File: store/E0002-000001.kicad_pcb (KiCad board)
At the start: 2 copper layers, 104.9 x 47 mm, 19 parts, among them J6 Seansor_Header_A, J7 Seansor_Header_B, U1 SHT45-AD1F-R2, U2 BME688, U3 SCD41-D-R2, U4 TLV70018, U5 NCP114

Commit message: M01: name the E0002 power nets GND and +3.3V
The straps are hard-tied to the rails (ADR-0014 d5), and the STRAP_x
global labels outranked the power symbols: the ground plane was named
STRAP_1, the 3V3 rail STRAP_0, and no GND net existed. The labels and
the tie block are removed; J7 pins 3, 4 and 5 tie to +3.3V, GND and GND
directly, with the strap pattern kept as schematic text.

Connectivity unchanged: 93 of 93 pad-to-net assignments identical under
the rename. ERC 21 -> 19, losing the two multiple_net_names warnings.
PCB nets renamed to match; DRC unchanged, parity clean.

Signed-off-by: IIchukissII <133657307+IIchukissII@users.noreply.github.com>
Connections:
- net STRAP_0 renamed +3.3V
- net STRAP_1 renamed GND

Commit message: Revert "M01: name the E0002 power nets GND and +3.3V"
This reverts f28e02d. The STRAP_x labels are back on the schematic and the
PCB nets are STRAP_1 and STRAP_0 again, at the same 168 and 70 references.

Also stores the DRC exclusion in the [key, comment] form KiCad itself
writes, replacing the bare string.

Signed-off-by: IIchukissII <133657307+IIchukissII@users.noreply.github.com>
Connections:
- net +3.3V renamed STRAP_0
- net GND renamed STRAP_1

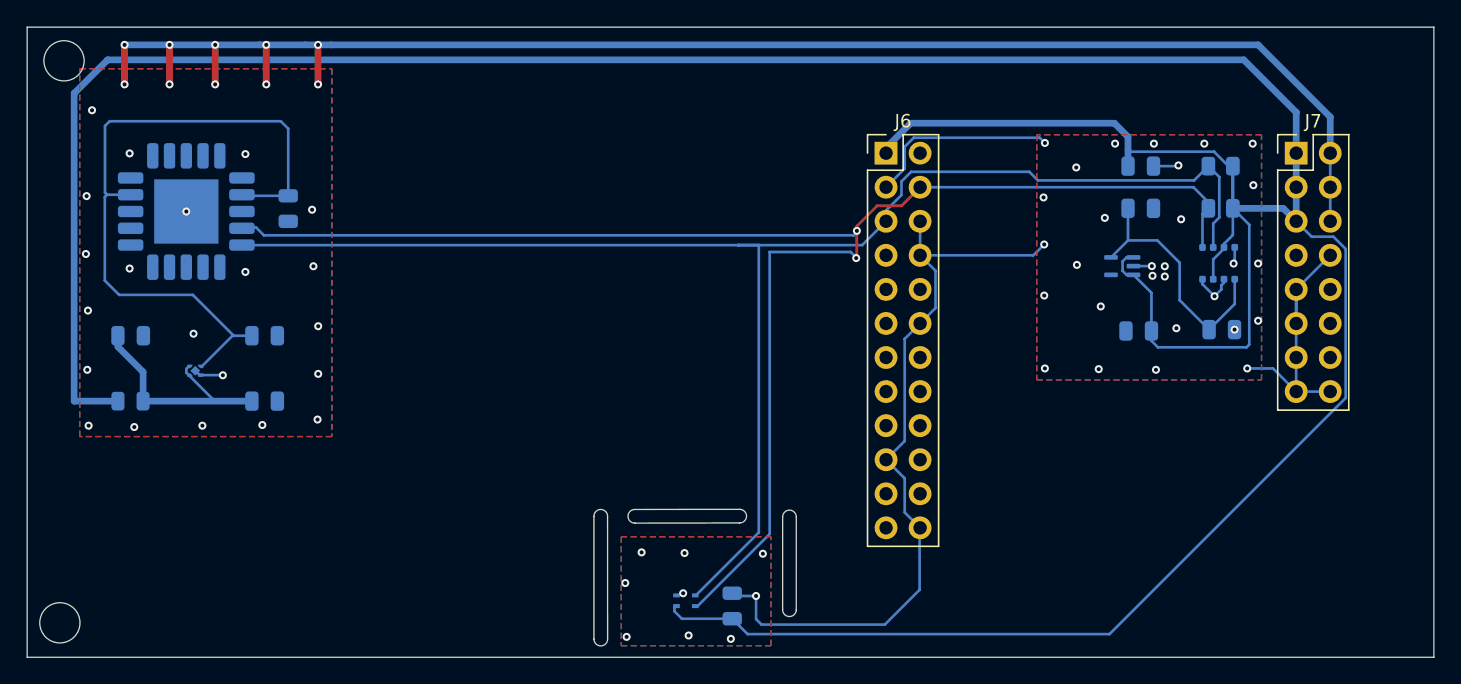
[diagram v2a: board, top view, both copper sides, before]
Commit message: M01: strap J7 pad 5 to GND so the module ID reads 0x01
Pad 5 carries module-ID bit 2 and was on the 3V3 net, which set the bit and
made the strap read 0b101 = 0x05 - the ID of M05-SAFETY, already fabricated
as E0006. The schematic had it on GND all along.

Pad 5 was also the only junction joining three parts of the 3V3 net, so both
branches are re-anchored to pad 3: the 0.5 mm trunk leaves pad 3 down-left to
the existing node at 170.2772,87.2744, and the 0.2 mm feed to U1 drops at
x=169.6772 to clear pad 5 before rejoining at 172.3904,89.3876. Pad 5 is
stitched across to pad 6 on GND.

Verified with zones refilled: 0 DRC violations, and parity drops from 4 to 3
as the net_conflict clears. The unconnected GND stub between pads 6 and 8 is
unchanged - the 3V3 feed to U1 crosses that column and still blocks it.

Signed-off-by: IIchukissII <133657307+IIchukissII@users.noreply.github.com>
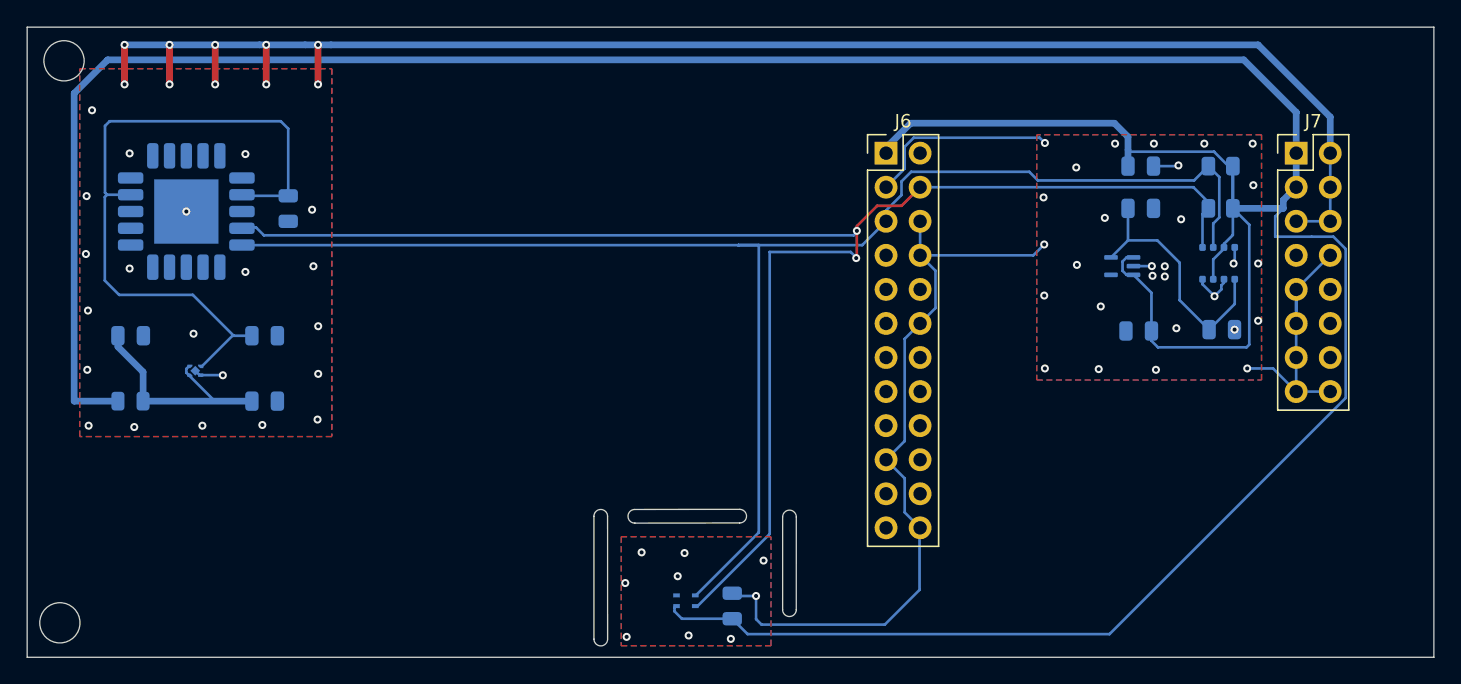
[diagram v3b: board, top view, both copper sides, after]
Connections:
- J7 pad 5: STRAP_0 -> STRAP_1
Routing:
- net STRAP_1: track 216.0 -> 218.5 mm
- net STRAP_0: track 276.1 -> 277.6 mm

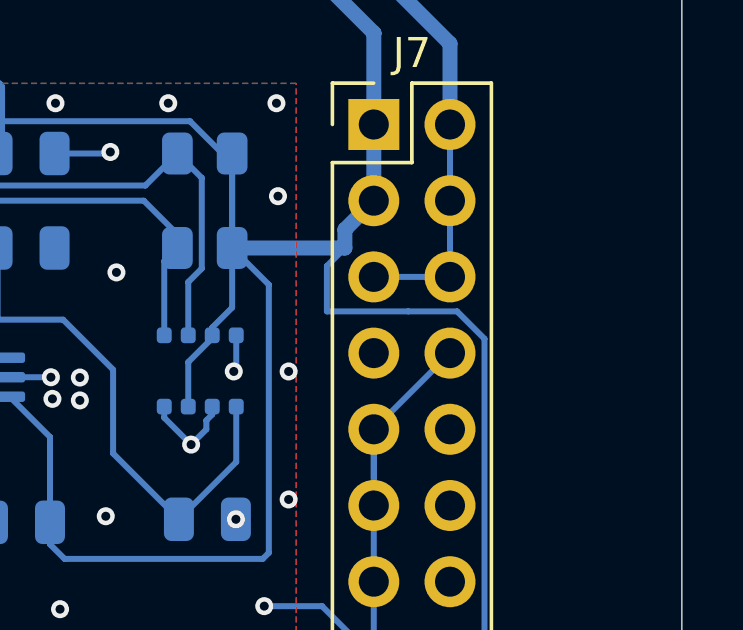
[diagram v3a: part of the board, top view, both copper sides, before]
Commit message: M01: bridge the J7 GND column on F.Cu
The 0.2 mm 3V3 feed to U1 crosses the even pad column on B.Cu at y=89.3876,
which left J7 pads 6 and 8 on separate GND islands. A 0.2 mm F.Cu run between
them clears it. J7 is a through-hole header, so its pads already reach F.Cu
and no vias are needed.

Verified with zones refilled: 0 DRC violations and 0 unconnected items. The
three remaining parity warnings are footprint Value fields holding the
reference designator.

Signed-off-by: IIchukissII <133657307+IIchukissII@users.noreply.github.com>
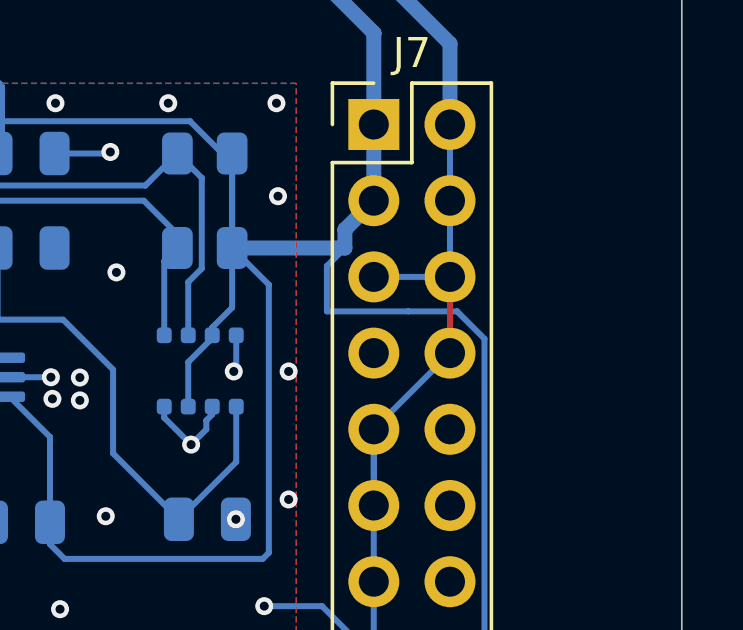
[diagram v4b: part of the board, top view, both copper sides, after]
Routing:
- net STRAP_1: track 218.5 -> 221.1 mm
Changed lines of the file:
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@@
+		(net "STRAP_1")
+	)
+	(segment
+		(start 173.7804 88.2376)
+		(end 173.7804 90.7776)
+		(width 0.2)
+		(layer "F.Cu")
 		(net "STRAP_1")
 	)

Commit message: M01: add the E0002 silkscreen logo and E-number
Copies the LOGO footprint and the E-number / SN text from E0006-000001, in
the arrangement that board uses: version and SN above the mark.

E0001 and E0006 carry all their parts on F.Cu and put the silkscreen on
F.SilkS. E0002 is the other way up - 17 of its 19 footprints are on B.Cu and
the front holds only J6 and J7 - so the block goes on B.SilkS, keeping it on
the component side. The footprint geometry is mirrored and the text carries
the mirror justify, so both read correctly on the back.

Placed at 118,95, in the clear area between the J6 column and the U3 group.
DRC unchanged at 0 violations and 0 unconnected, with no silk_over_copper,
silk_overlap or silk_edge_clearance warnings.

Signed-off-by: IIchukissII <133657307+IIchukissII@users.noreply.github.com>
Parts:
- added G***: LOGO, LOGO, B.Cu at (118.0, 95.0)
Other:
- board text added: "E0002 V00.00.01"
- board text added: "SN:"
